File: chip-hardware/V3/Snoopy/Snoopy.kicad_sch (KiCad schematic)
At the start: 6 parts

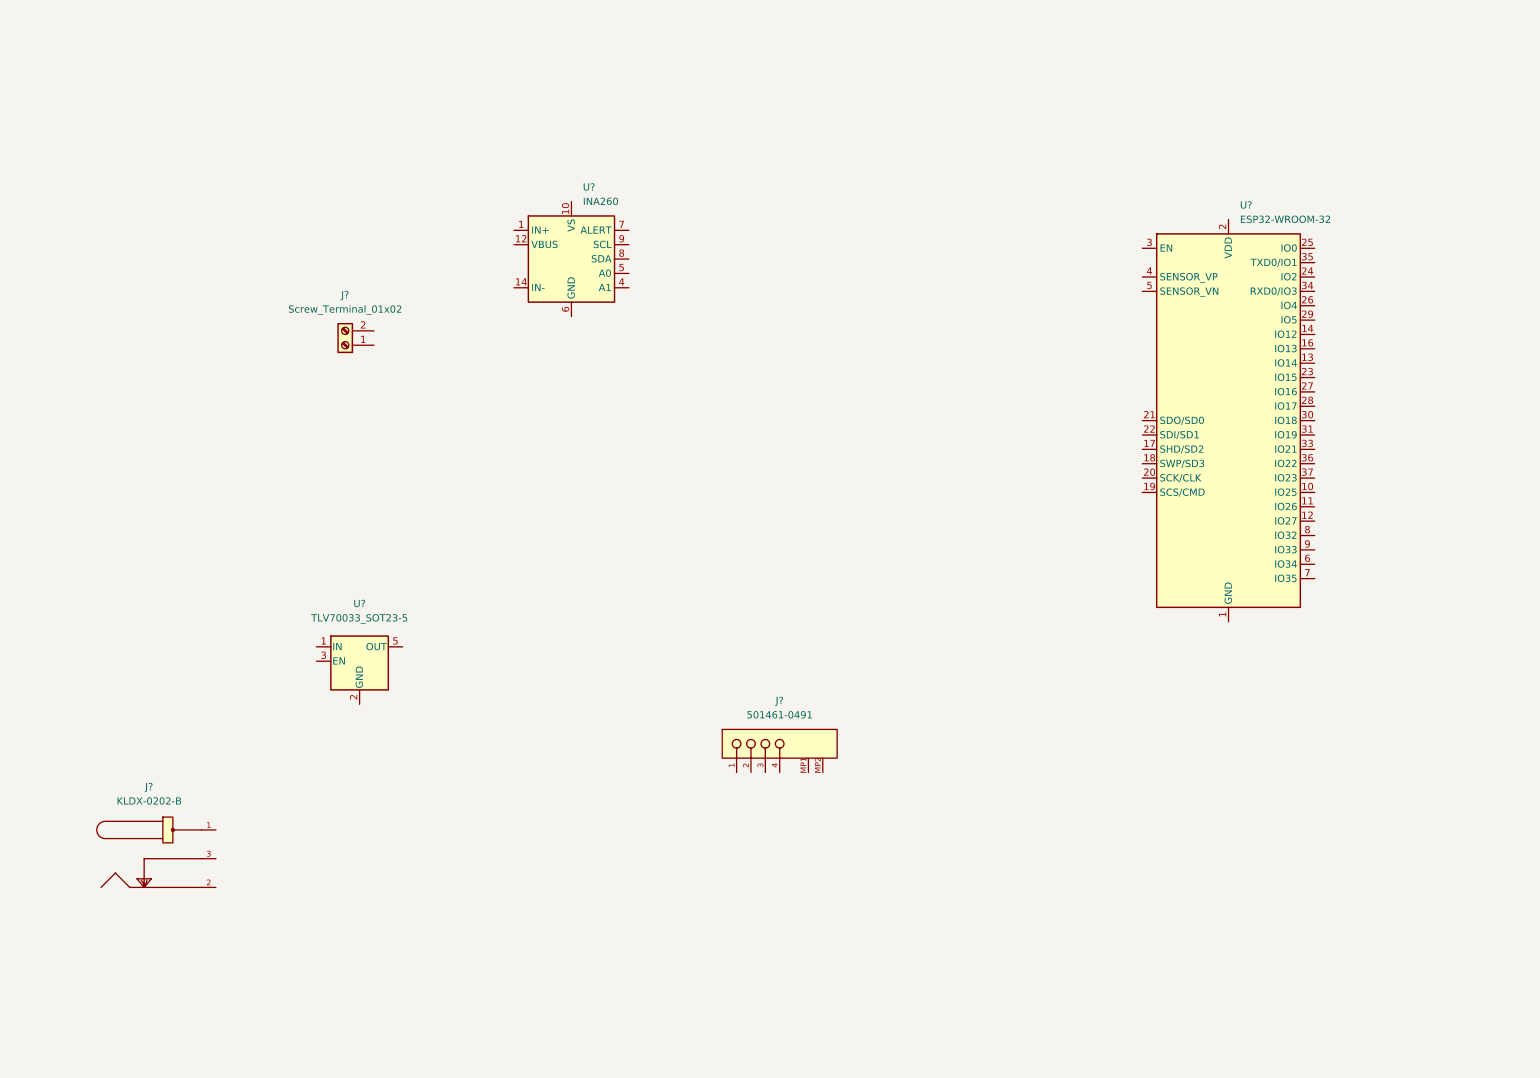
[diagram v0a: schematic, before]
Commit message: Finished layout of componets on sch
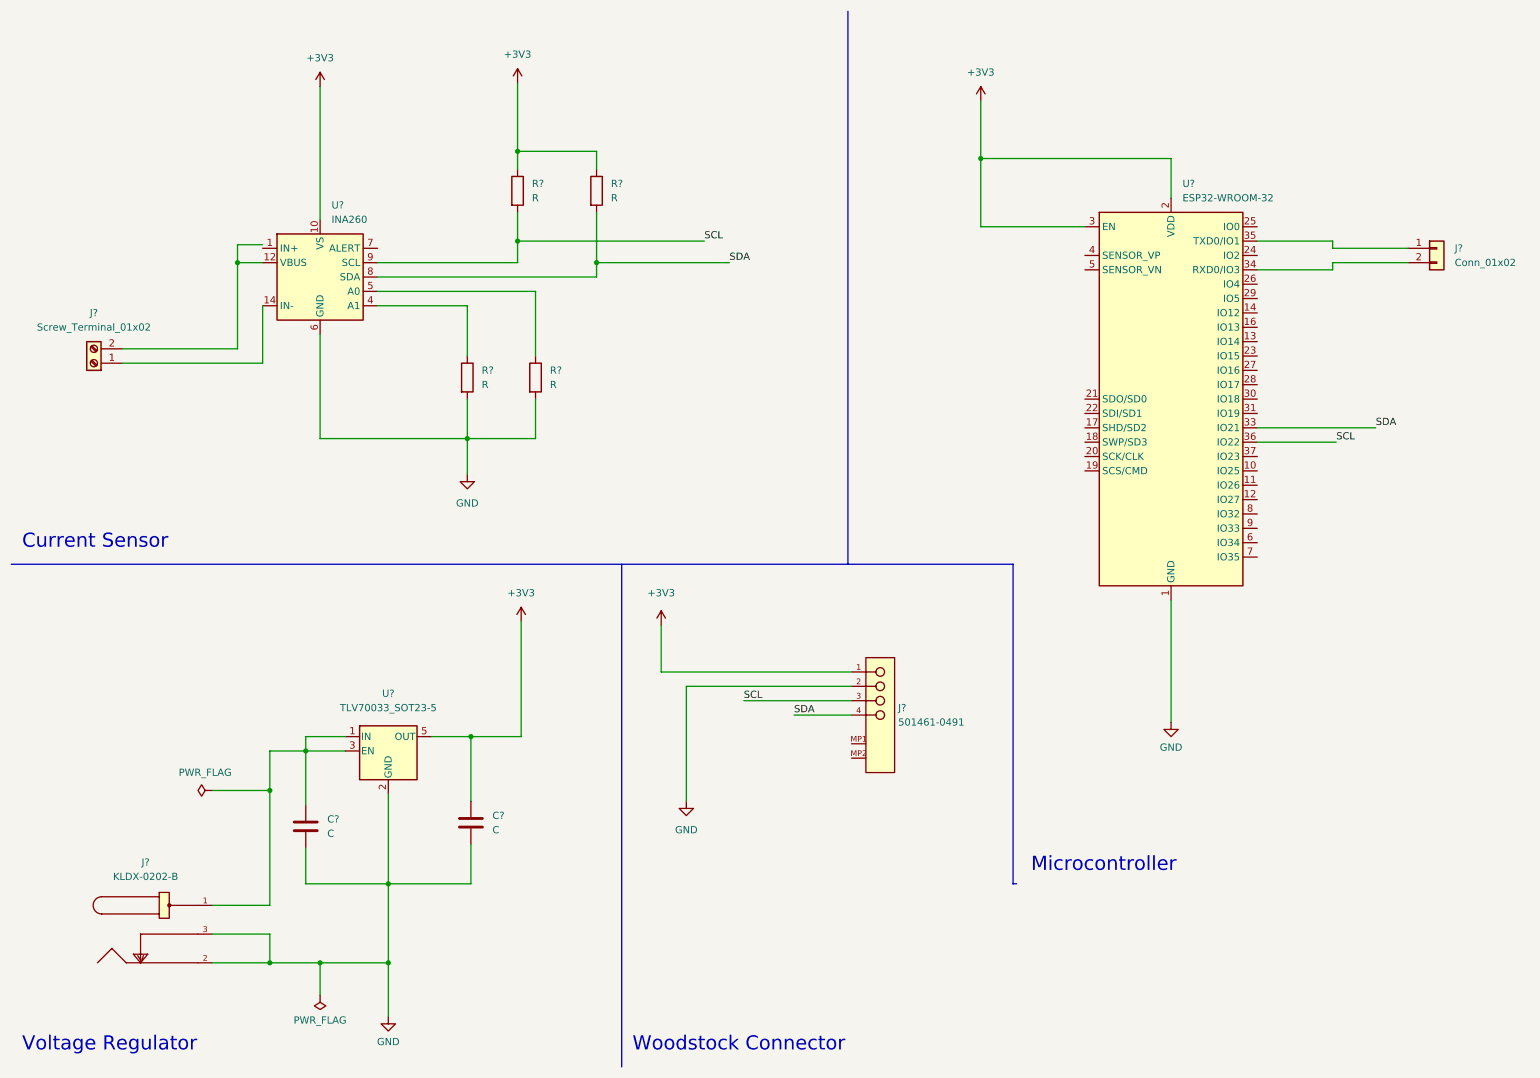
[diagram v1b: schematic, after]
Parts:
- added C? (x2): C, symbol Device:C
- added J?: Conn_01x02, symbol Connector_Generic:Conn_01x02
- added R? (x4): R, symbol Device:R
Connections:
- net GND: now reaches U?.1 (GND), U?.15 (GND), U?.38 (GND), U?.39 (GND)
- net GND: now also J?.2, J?.2, J?.3, U?.11 (GND), U?.2 (GND), U?.6 (GND), C?.2, C?.2, R?.2, R?.2
- net +3V3: now reaches U?.2 (VDD)
- net +3V3: now also J?.1, U?.10 (VS), U?.3 (EN), U?.5 (OUT), C?.1, R?.1, R?.1
- net SDA: now reaches U?.33 (IO21)
- net SDA: now also J?.4, U?.8 (SDA), R?.2
- net at U?.34 (RXD0/IO3): now also J?.2 (Pin_2)
- net at U?.35 (TXD0/IO1): now also J?.1 (Pin_1)
- net SCL: now reaches U?.36 (IO22)
- net SCL: now also J?.3, U?.9 (SCL), R?.2
- net at U?.1 (IN): now also J?.1, U?.3 (EN), C?.1
- net at J?.1 (Pin_1): now also U?.14 (IN-), U?.15 (IN-), U?.16 (IN-)
- net at J?.2 (Pin_2): now also U?.12 (VBUS)
- net at U?.4 (A1): now also R?.1
- net at U?.5 (A0): now also R?.1
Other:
- note added: "Current Sensor"
- note added: "Microcontroller"
- note added: "Voltage Regulator"
- note added: "Woodstock Connector"
- moved on the sheet: J?, U?

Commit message: Got the rest of the parts worked out
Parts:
- C1: renamed from C?; value C -> 10uF; footprint (none) -> Capacitor_SMD:C_0603_1608Metric_Pad1.08x0.95mm_HandSolder
- C2: renamed from C?; value C -> 1uF; footprint (none) -> Capacitor_SMD:C_0603_1608Metric_Pad1.08x0.95mm_HandSolder
- J1: renamed from J?; footprint (none) -> TerminalBlock_RND:TerminalBlock_RND_205-00232_1x02_P5.08mm_Horizontal
- J2: renamed from J?; footprint Kycon-KLDX-0202-B-* -> KLDX-0202-B:Kycon-KLDX-0202-B-MFG
- J3: renamed from J?; footprint Molex-501461-0491-* -> 5014610491:Molex-501461-0491-Manufacturer_Recommended
- J4: renamed from J?; footprint (none) -> Connector_Wago:Wago_734-162_1x02_P3.50mm_Horizontal
- R1, R2, R3, R4: renamed from R?; value R -> 10k; footprint (none) -> Resistor_SMD:R_0603_1608Metric_Pad0.98x0.95mm_HandSolder
- gave numbers to parts that had none: 3

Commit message: Added adjustment to the PCB. Everything seems right
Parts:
- J4: footprint Connector_Wago:Wago_734-162_1x02_P3.50mm_Horizontal -> Connector_Wire:SolderWire-0.1sqmm_1x02_P3.6mm_D0.4mm_OD1mm
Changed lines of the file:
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@@
       (effects (font (size 1.27 1.27)) (justify left))
     )
-    (property "Footprint" "Connector_Wago:Wago_734-162_1x02_P3.50mm_Horizontal" (id 2) (at 264.16 53.34 0)
+    (property "Footprint" "Connector_Wire:SolderWire-0.1sqmm_1x02_P3.6mm_D0.4mm_OD1mm" (id 2) (at 264.16 53.34 0)
       (effects (font (size 1.27 1.27)) hide)
     )
@@
     )
     (path "/0153a7f3-f3ea-4b25-a0c4-092faa2372f5"
-      (reference "J4") (unit 1) (value "Conn_01x02") (footprint "Connector_Wago:Wago_734-162_1x02_P3.50mm_Horizontal")
+      (reference "J4") (unit 1) (value "Conn_01x02") (footprint "Connector_Wire:SolderWire-0.1sqmm_1x02_P3.6mm_D0.4mm_OD1mm")
     )
     (path "/10477cb7-baf7-4ecc-b98f-6ce44d7a2159"
